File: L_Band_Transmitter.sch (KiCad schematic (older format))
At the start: 1 part

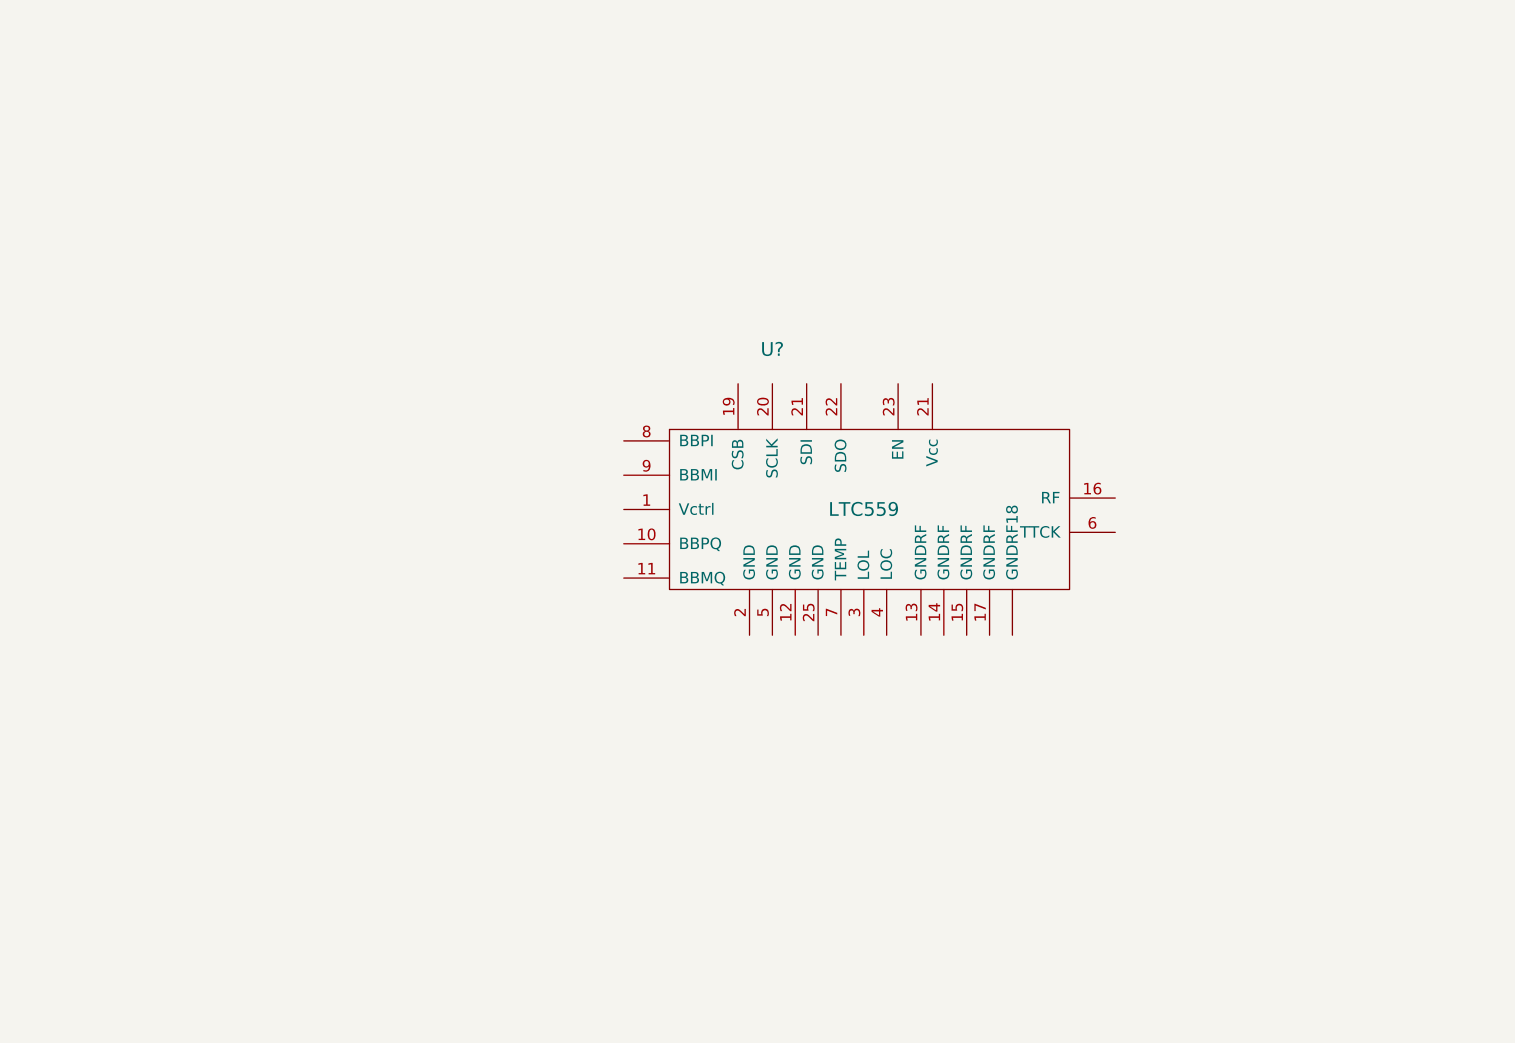
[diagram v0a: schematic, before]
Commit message: Created lib components
LTC5599 SI535 and STM32 connector
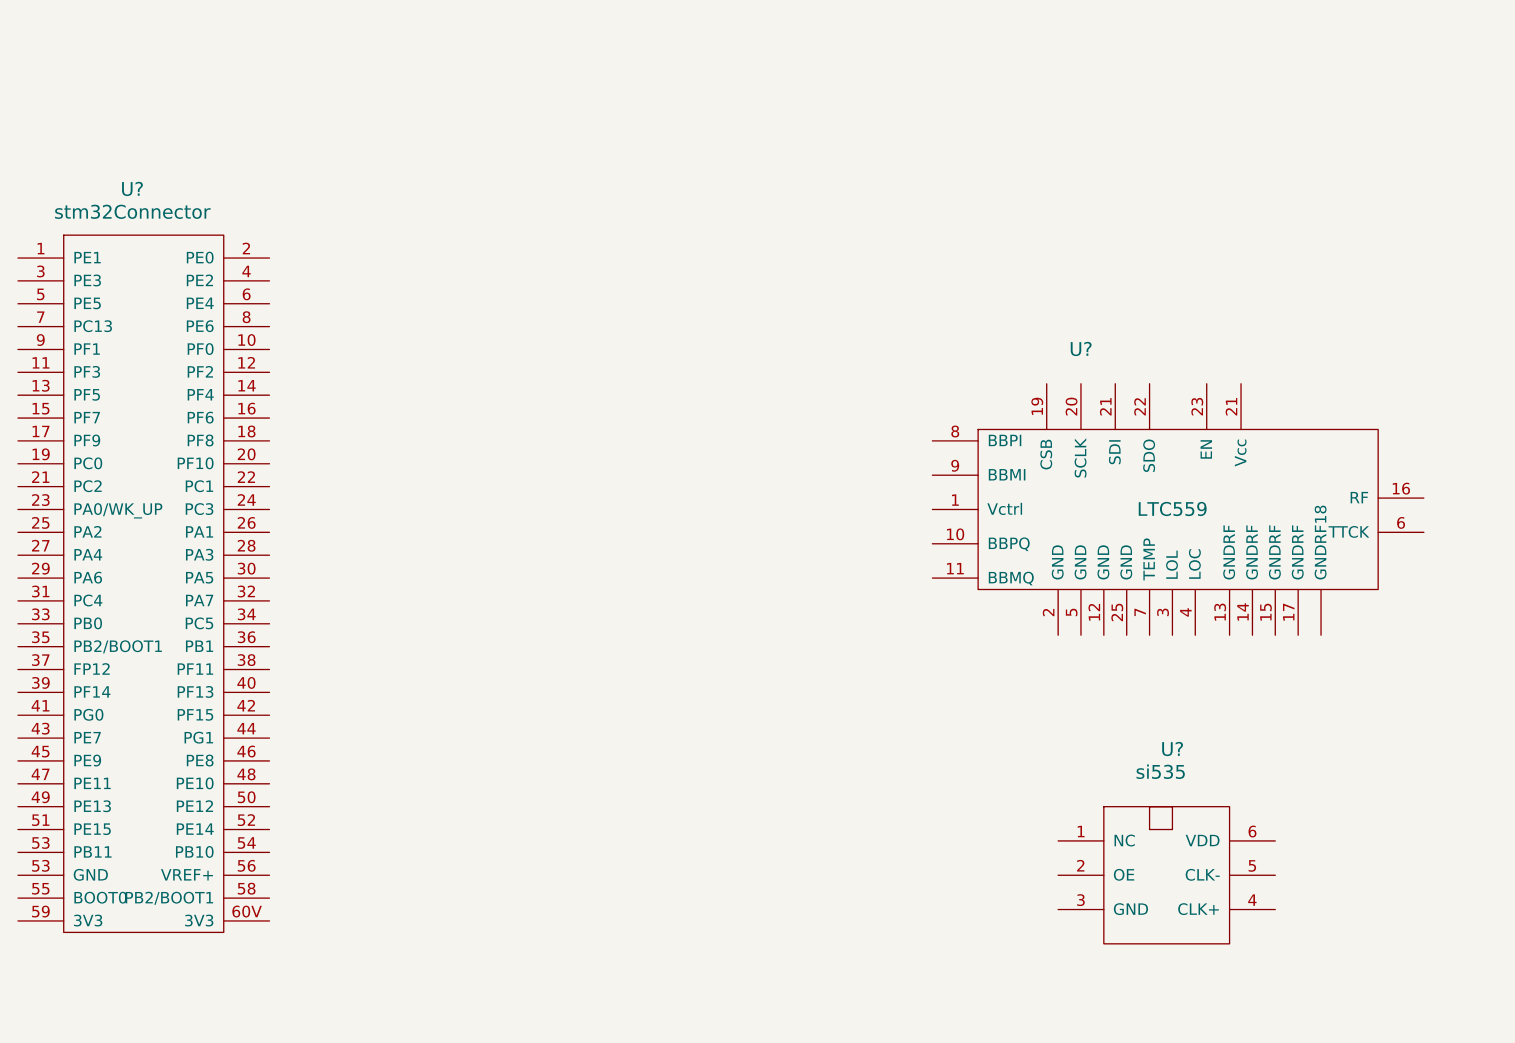
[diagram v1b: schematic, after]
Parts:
- added U?: stm32Connector, symbol stm32Connector
- added U?: si535, symbol si535
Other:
- moved on the sheet: U?
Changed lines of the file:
@@
 LIBS:valves
 LIBS:ltc559
+LIBS:STM32407_J2_Connector
+LIBS:SI535
+LIBS:L_Band_Transmitter-cache
 EELAYER 25 0
 EELAYER END
@@
 encoding utf-8
 Sheet 1 1
-Title ""
-Date ""
-Rev ""
-Comp ""
-Comment1 ""
+Title "L Band Transmitter"
+Date "2017-02-08"
+Rev "Rev1.0"
+Comp "Giga Technology"
+Comment1 "1.2 Ghz L Band Transmitter"
 Comment2 ""
 Comment3 ""
@@
 L LTC559 U?
 U 1 1 589B6F62
-P 5500 3300
-F 0 "U?" H 5400 3850 60  0000 C CNN
-F 1 "LTC559" H 5800 3150 60  0000 C CNN
-F 2 "" H 5400 3250 60  0000 C CNN
-F 3 "" H 5400 3250 60  0000 C CNN
-	1    5500 3300
+P 6850 3300
+F 0 "U?" H 6750 3850 60  0000 C CNN
+F 1 "LTC559" H 7150 3150 60  0000 C CNN
+F 2 "" H 6750 3250 60  0000 C CNN
+F 3 "" H 6750 3250 60  0000 C CNN
+	1    6850 3300
 	1    0    0    -1
 $EndComp
+$Comp
+L stm32Connector U?
+U 1 1 589B8CE4
+P 2650 3750
+F 0 "U?" H 2600 5450 60  0000 C CNN
+F 1 "stm32Connector" H 2600 5350 60  0000 C CNN
+F 2 "" H 2400 4750 60  0000 C CNN
+F 3 "" H 2400 4750 60  0000 C CNN
+	1    2650 3750
+	1    0    0    -1
+$EndComp
+$Comp
+L si535 U?
+U 1 1 589B8F46
+P 7100 5050
+F 0 "U?" H 7150 5600 60  0000 C CNN
+F 1 "si535" H 7100 5500 60  0000 C CNN
+F 2 "" H 7100 5150 60  0000 C CNN
+F 3 "" H 7100 5150 60  0000 C CNN
+	1    7100 5050
+	1    0    0    -1
+$EndComp

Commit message: Added new Lib and updated SCH
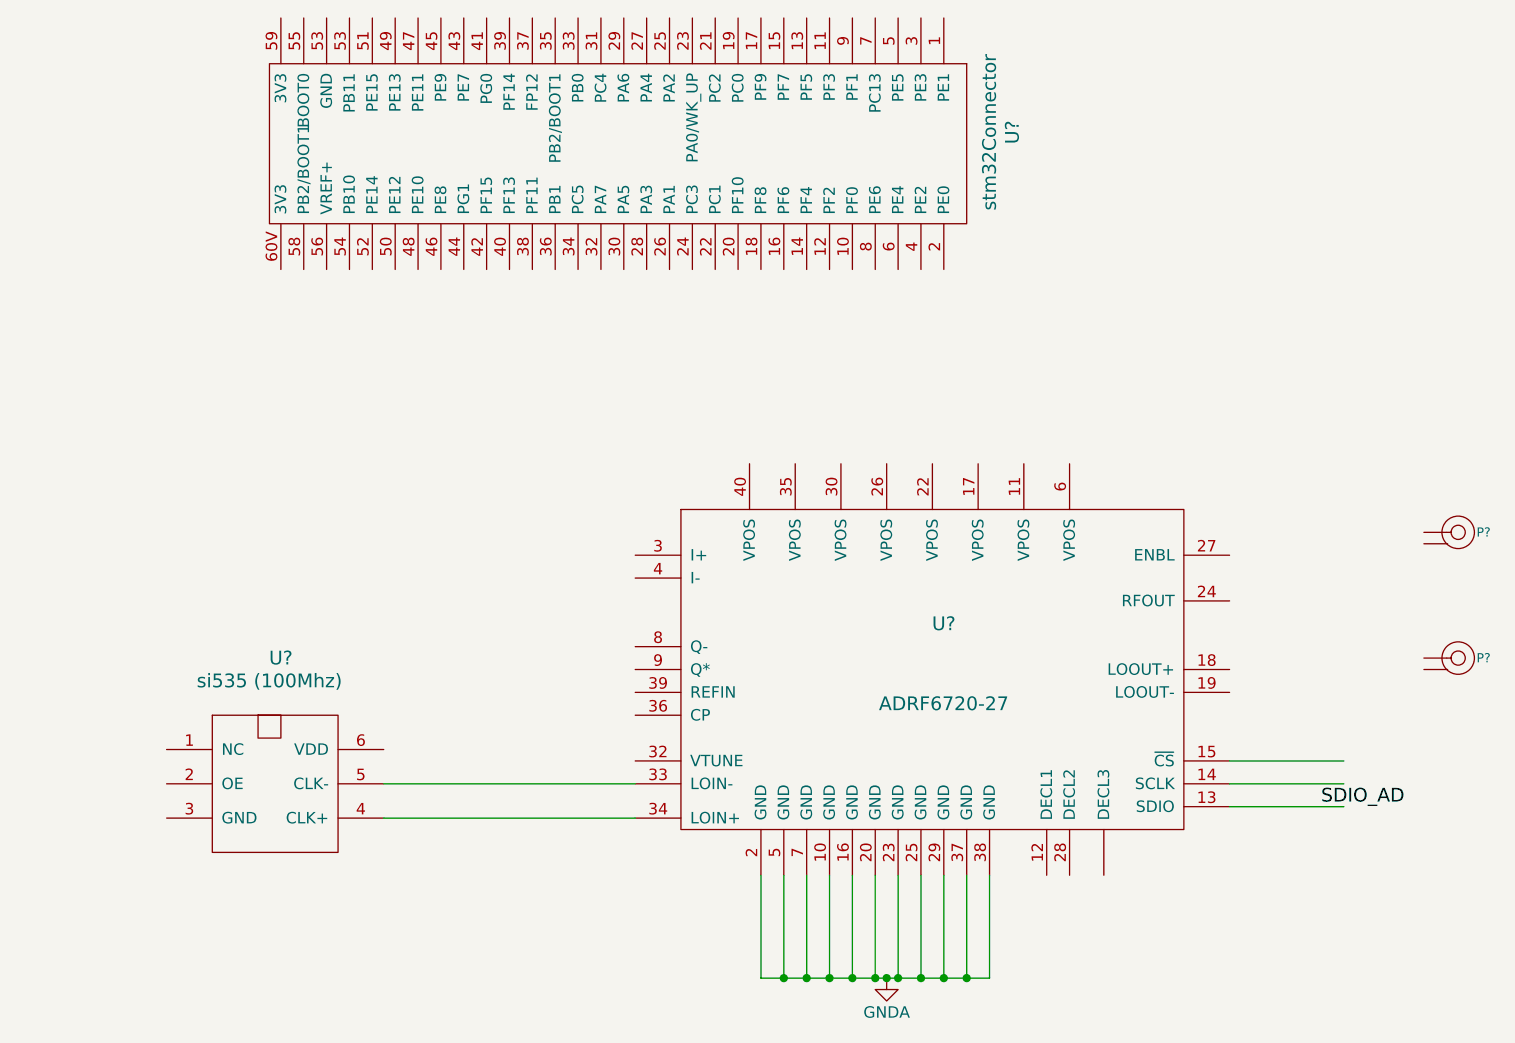
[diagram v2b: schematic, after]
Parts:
- removed U?: LTC559, symbol LTC559
- added P?: SMA RF Out, symbol SMA
- added P?: SMA LO Out, symbol SMA
- added U?: ADRF6720-27, symbol ADRF6720-27
- U?: value si535 -> si535 (100Mhz)
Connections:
- net labels added: GNDA, SDIO_AD
- wire segments 0 -> 17
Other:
- moved on the sheet: U?
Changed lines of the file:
@@
 LIBS:STM32407_J2_Connector
 LIBS:SI535
+LIBS:ADRF6720-27
+LIBS:Raspberry_Pi_2m_TX_LPF_7Stage-cache
+LIBS:Raspberry_Pi_2m_TX-cache
+LIBS:RPi_Hat-cache
 LIBS:L_Band_Transmitter-cache
 EELAYER 25 0
@@
 $EndDescr
 $Comp
-L LTC559 U?
-U 1 1 589B6F62
-P 6850 3300
-F 0 "U?" H 6750 3850 60  0000 C CNN
-F 1 "LTC559" H 7150 3150 60  0000 C CNN
-F 2 "" H 6750 3250 60  0000 C CNN
-F 3 "" H 6750 3250 60  0000 C CNN
-	1    6850 3300
-	1    0    0    -1
-$EndComp
-$Comp
 L stm32Connector U?
 U 1 1 589B8CE4
-P 2650 3750
-F 0 "U?" H 2600 5450 60  0000 C CNN
-F 1 "stm32Connector" H 2600 5350 60  0000 C CNN
-F 2 "" H 2400 4750 60  0000 C CNN
-F 3 "" H 2400 4750 60  0000 C CNN
-	1    2650 3750
-	1    0    0    -1
+P 4750 1850
+F 0 "U?" H 4700 3550 60  0000 C CNN
+F 1 "stm32Connector" H 4700 3450 60  0000 C CNN
+F 2 "" H 4500 2850 60  0000 C CNN
+F 3 "" H 4500 2850 60  0000 C CNN
+	1    4750 1850
+	0    1    1    0
 $EndComp
 $Comp
 L si535 U?
 U 1 1 589B8F46
-P 7100 5050
-F 0 "U?" H 7150 5600 60  0000 C CNN
-F 1 "si535" H 7100 5500 60  0000 C CNN
-F 2 "" H 7100 5150 60  0000 C CNN
-F 3 "" H 7100 5150 60  0000 C CNN
-	1    7100 5050
+P 3200 4650
+F 0 "U?" H 3250 5200 60  0000 C CNN
+F 1 "si535 (100Mhz)" H 3200 5100 60  0000 C CNN
+F 2 "" H 3200 4750 60  0000 C CNN
+F 3 "" H 3200 4750 60  0000 C CNN
+	1    3200 4650
 	1    0    0    -1
 $EndComp
+$Comp
+L ADRF6720-27 U?
+U 1 1 58A4AC79
+P 6150 4200
+F 0 "U?" H 6150 4450 60  0000 C CNN
+F 1 "ADRF6720-27" H 6150 4100 60  0000 C CNN
+F 2 "" H 5700 4050 60  0000 C CNN
+F 3 "" H 5700 4050 60  0000 C CNN
+	1    6150 4200
+	1    0    0    -1
+$EndComp
+$Comp
+L SMA P?
+U 1 1 58A4AF14
+P 8400 3550
+F 0 "P?" H 8480 3550 40  0000 L CNN
+F 1 "SMA RF Out" H 8400 3605 30  0001 C TNN
+F 2 "" H 8400 3550 60  0000 C CNN
+F 3 "" H 8400 3550 60  0000 C CNN
+	1    8400 3550
+	1    0    0    -1
+$EndComp
+$Comp
+L SMA P?
+U 1 1 58A4AFC9
+P 8400 4100
+F 0 "P?" H 8480 4100 40  0000 L CNN
+F 1 "SMA LO Out" H 8400 4155 30  0001 C TNN
+F 2 "" H 8400 4100 60  0000 C CNN
+F 3 "" H 8400 4100 60  0000 C CNN
+	1    8400 4100
+	1    0    0    -1
+$EndComp
+$Comp
+L GNDA #PWR?
+U 1 1 58A4B907
+P 5900 5500
+F 0 "#PWR?" H 5900 5250 50  0001 C CNN
+F 1 "GNDA" H 5900 5350 50  0000 C CNN
+F 2 "" H 5900 5500 50  0000 C CNN
+F 3 "" H 5900 5500 50  0000 C CNN
+	1    5900 5500
+	1    0    0    -1
+$EndComp
+Wire Wire Line
+	3700 4650 4800 4650
+Wire Wire Line
+	4800 4800 3700 4800
+Wire Wire Line
+	5350 5500 6350 5500
+Wire Wire Line
+	5350 5500 5350 5050
+Wire Wire Line
+	5450 5050 5450 5500
+Connection ~ 5450 5500
+Wire Wire Line
+	5550 5050 5550 5500
+Connection ~ 5550 5500
+Wire Wire Line
+	5650 5050 5650 5500
+Connection ~ 5650 5500
+Wire Wire Line
+	5750 5050 5750 5500
+Connection ~ 5750 5500
+Wire Wire Line
+	5850 5050 5850 5500
+Connection ~ 5850 5500
+Wire Wire Line
+	6350 5500 6350 5050
+Connection ~ 5900 5500
+Wire Wire Line
+	6250 5050 6250 5500
+Connection ~ 6250 5500
+Wire Wire Line
+	6150 5050 6150 5500
+Connection ~ 6150 5500
+Wire Wire Line
+	6050 5050 6050 5500
+Connection ~ 6050 5500
+Wire Wire Line
+	5950 5050 5950 5500
+Connection ~ 5950 5500
+Text Label 7800 4750 0    60   ~ 0
+SDIO_AD
+Wire Wire Line
+	7400 4750 7900 4750
+Wire Wire Line
+	7400 4650 7900 4650
+Wire Wire Line
+	7400 4550 7900 4550
 $EndSCHEMATC
